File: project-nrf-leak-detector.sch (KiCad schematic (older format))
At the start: 16 parts, among them J1 Conn_02x05_Odd_Even, U1 MS88SF3_NRF52840

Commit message: Add a few more components to the schematic
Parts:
- added D?: D_Schottky, CUS10S30,H3F:DIO_CUS520,H3F, symbol Device:D_Schottky
- added L?: L, 22R686MC:INDP7870X750, symbol Device:L
- added Q?: Q_NMOS_GSD, Package_TO_SOT_SMD:SOT-323_SC-70, symbol Device:Q_NMOS_GSD
- added R?: 10k, Resistor_SMD:R_0603_1608Metric, symbol Device:R
- R1: value 5.1k -> 10k
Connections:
- net labels added: BUZZER, VBATT_PROBE, WATER_PROBE, ~RESET
- net labels removed: AIN0, AIN1, AIN2, AIN3, AIN5, NFC1, NFC2, P0.13, RESET
- wire segments 100 -> 98
- no-connect marks 28 -> 26
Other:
- note added: "Battery Voltage Reading"
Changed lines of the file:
@@
 $EndComp
 Text Label 1350 6600 0    50   ~ 0
-RESET
+~RESET
 $Comp
 L Device:R R1
@@
 P 1850 6350
 F 0 "R1" H 1920 6396 50  0000 L CNN
-F 1 "5.1k" H 1920 6305 50  0000 L CNN
+F 1 "10k" H 1920 6305 50  0000 L CNN
 F 2 "Resistor_SMD:R_0603_1608Metric" V 1780 6350 50  0001 C CNN
 F 3 "~" H 1850 6350 50  0001 C CNN
@@
 	3250 6600 3250 7100
 Text Label 6450 4550 2    50   ~ 0
-RESET
+~RESET
 Wire Wire Line
 	6450 4550 6100 4550
@@
 Wire Wire Line
 	3950 4400 3600 4400
-Text Label 850  2500 0    50   ~ 0
-AIN0
-Wire Wire Line
-	850  2500 1200 2500
-Text Label 3950 2700 2    50   ~ 0
-AIN5
-Wire Wire Line
-	3950 2700 3600 2700
-Text Label 850  2800 0    50   ~ 0
-AIN3
-Wire Wire Line
-	850  2800 1200 2800
-Text Label 850  2700 0    50   ~ 0
-AIN2
-Wire Wire Line
-	850  2700 1200 2700
-Text Label 850  3300 0    50   ~ 0
-NFC2
-Wire Wire Line
-	850  3300 1200 3300
-Text Label 850  3200 0    50   ~ 0
-NFC1
-Wire Wire Line
-	850  3200 1200 3200
+Text Label 650  2500 0    50   ~ 0
+WATER_PROBE
+Wire Wire Line
+	650  2500 1200 2500
+Text Label 650  2700 0    50   ~ 0
+VBATT_PROBE
+Wire Wire Line
+	650  2700 1200 2700
 Text Label 3950 2300 2    50   ~ 0
 P0.25
@@
 D_P
 Text Label 850  4100 0    50   ~ 0
-RESET
+~RESET
 Wire Wire Line
 	850  4100 1200 4100
@@
 Wire Wire Line
 	850  3800 1200 3800
-Text Label 850  3600 0    50   ~ 0
-P0.13
-Wire Wire Line
-	850  3600 1200 3600
+Text Label 850  2900 0    50   ~ 0
+BUZZER
+Wire Wire Line
+	850  2900 1200 2900
 Text Label 850  4200 0    50   ~ 0
 P0.19
@@
 	1    0    0    -1
 $EndComp
-Text Label 850  2600 0    50   ~ 0
-AIN1
-Wire Wire Line
-	850  2600 1200 2600
 NoConn ~ 1200 1800
 NoConn ~ 1200 2300
 NoConn ~ 1200 2400
-NoConn ~ 1200 2900
 NoConn ~ 1200 3000
 NoConn ~ 1200 3100
@@
 NoConn ~ 3600 2400
 NoConn ~ 3600 2500
-NoConn ~ 3600 2600
 NoConn ~ 3600 2800
 NoConn ~ 3600 2900
@@
 	1    0    0    -1
 $EndComp
+Text Notes 7050 3750 0    50   ~ 0
+Battery Voltage Reading
+Text Label 7200 4100 0    50   ~ 0
+VBATT_PROBE
+Wire Wire Line
+	7750 4100 7200 4100
+Text Label 9600 2700 0    50   ~ 0
+WATER_PROBE
+Wire Wire Line
+	9600 2700 10150 2700
+$Comp
+L Device:Q_NMOS_GSD Q?
+U 1 1 6387FC80
+P 5450 1900
+F 0 "Q?" H 5655 1900 50  0000 L CNN
+F 1 "Q_NMOS_GSD" H 5654 1855 50  0001 L CNN
+F 2 "Package_TO_SOT_SMD:SOT-323_SC-70" H 5650 2000 50  0001 C CNN
+F 3 "~" H 5450 1900 50  0001 C CNN
+	1    5450 1900
+	1    0    0    -1
+$EndComp
+$Comp
+L Device:D_Schottky D?
+U 1 1 6388212A
+P 5450 2550
+F 0 "D?" H 5450 2675 50  0000 C CNN
+F 1 "D_Schottky" H 5450 2676 50  0001 C CNN
+F 2 "CUS10S30,H3F:DIO_CUS520,H3F" H 5450 2550 50  0001 C CNN
+F 3 "~" H 5450 2550 50  0001 C CNN
+	1    5450 2550
+	1    0    0    -1
+$EndComp
+$Comp
+L Device:L L?
+U 1 1 638880E9
+P 6000 2400
+F 0 "L?" H 6053 2446 50  0000 L CNN
+F 1 "L" H 6053 2355 50  0000 L CNN
+F 2 "22R686MC:INDP7870X750" H 6000 2400 50  0001 C CNN
+F 3 "~" H 6000 2400 50  0001 C CNN
+	1    6000 2400
+	1    0    0    -1
+$EndComp
+$Comp
+L Device:R R?
+U 1 1 6388DC50
+P 4950 2150
+F 0 "R?" H 5020 2196 50  0000 L CNN
+F 1 "10k" H 5020 2105 50  0000 L CNN
+F 2 "Resistor_SMD:R_0603_1608Metric" V 4880 2150 50  0001 C CNN
+F 3 "~" H 4950 2150 50  0001 C CNN
+	1    4950 2150
+	1    0    0    -1
+$EndComp
+$Comp
+L power:GND #PWR?
+U 1 1 63892E4C
+P 4950 2450
+F 0 "#PWR?" H 4950 2200 50  0001 C CNN
+F 1 "GND" H 4955 2277 50  0000 C CNN
+F 2 "" H 4950 2450 50  0001 C CNN
+F 3 "" H 4950 2450 50  0001 C CNN
+	1    4950 2450
+	1    0    0    -1
+$EndComp
+Text Label 4800 1650 0    50   ~ 0
+BUZZER
+Wire Wire Line
+	4800 1650 5150 1650
 $EndSCHEMATC

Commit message: First schematic version
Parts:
- removed C6: 4.7uF, Capacitor_SMD:C_0805_2012Metric, symbol Device:C
- removed JP1: SolderJumper_2_Bridged, Jumper:SolderJumper-2_P1.3mm_Bridged_RoundedPad1.0x1.5mm, symbol Jumper:SolderJumper_2_Bridged
- removed JP2: SolderJumper_2_Open, Jumper:SolderJumper-2_P1.3mm_Open_RoundedPad1.0x1.5mm, symbol Jumper:SolderJumper_2_Open
- removed L1: 10uH, Inductor_SMD:L_0603_1608Metric, symbol Device:L
- removed R3: 4.7, Resistor_SMD:R_0603_1608Metric, symbol Device:R
- added R?: 10k, Resistor_SMD:R_0603_1608Metric, symbol Device:R
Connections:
- net labels added: VDD
- net labels removed: DCCH, D_N, D_P, P0.15, P0.17, P0.19, P0.21, P0.22, P0.23, P0.25, P1.10, P1.13, P1.14, P1.15, VBATT_PROBE, VBUS, VBUS_nRF, VDDH
- wire segments 98 -> 71
- no-connect marks 26 -> 47
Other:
- note added: "Normal Voltage Mode\nLDO only"
- note removed: "(VDD OUT)"
- note removed: "Battery Voltage Reading"
- note removed: "PCA10059\nRevision: 2.0.0\n17.09.2020"
- note removed: "Power Input Choice"
- moved on the sheet: BT?, C2, D?, J?, L?, LS?, Q?, R?

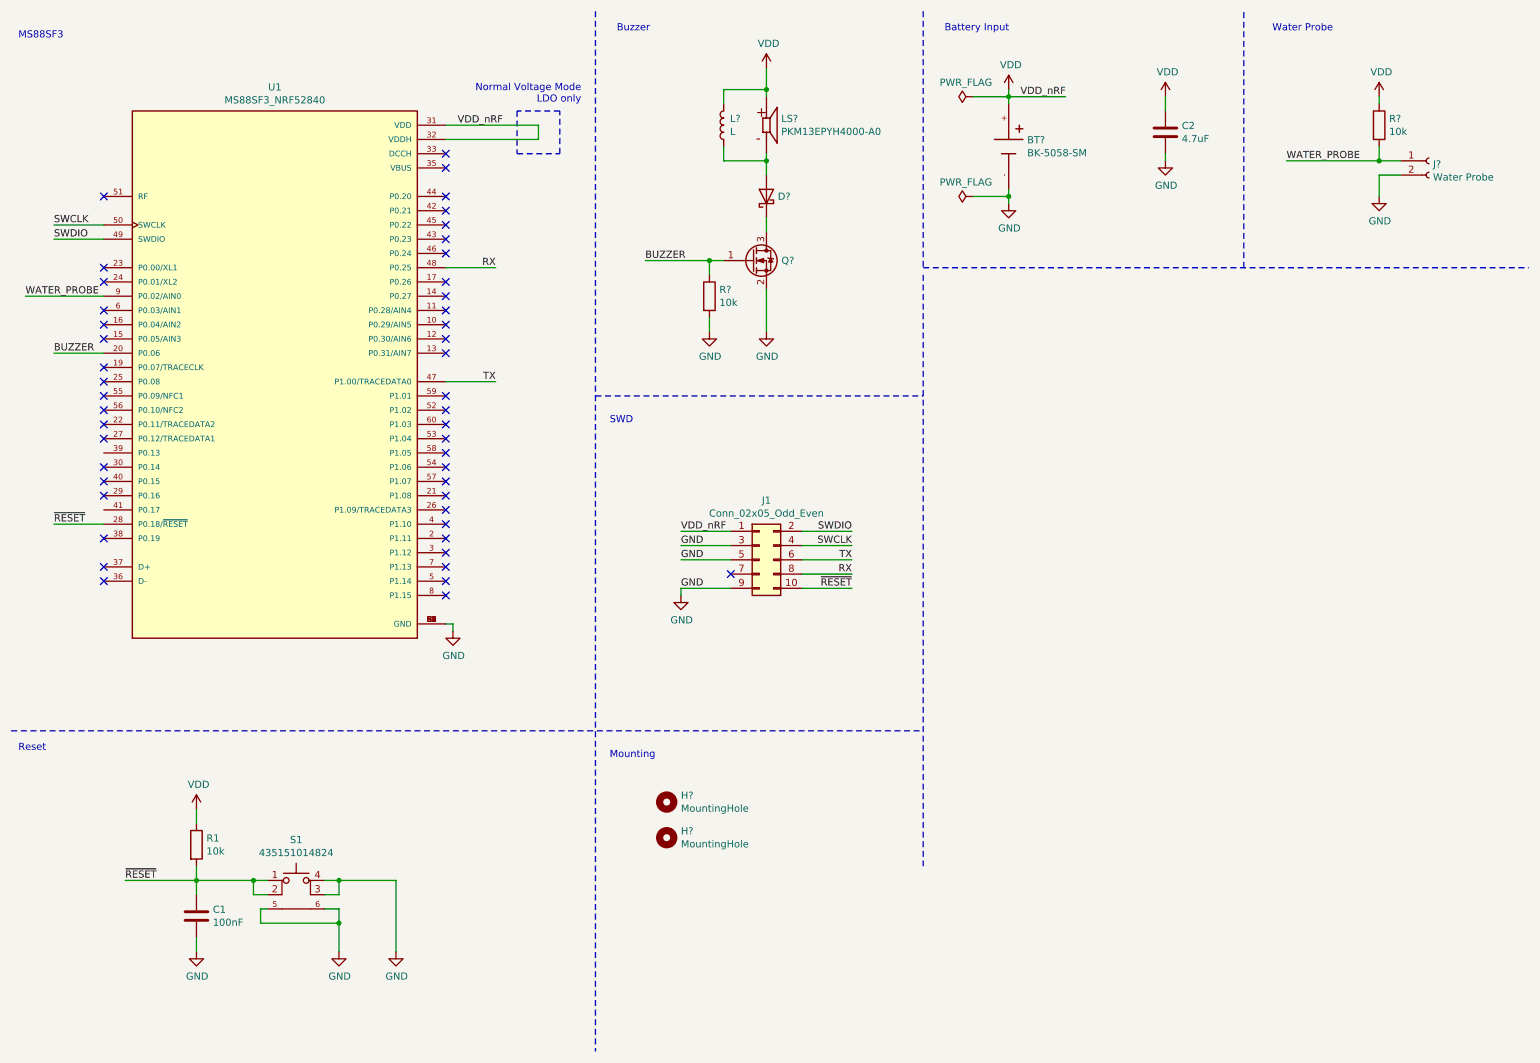
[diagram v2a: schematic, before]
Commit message: Import parts to board
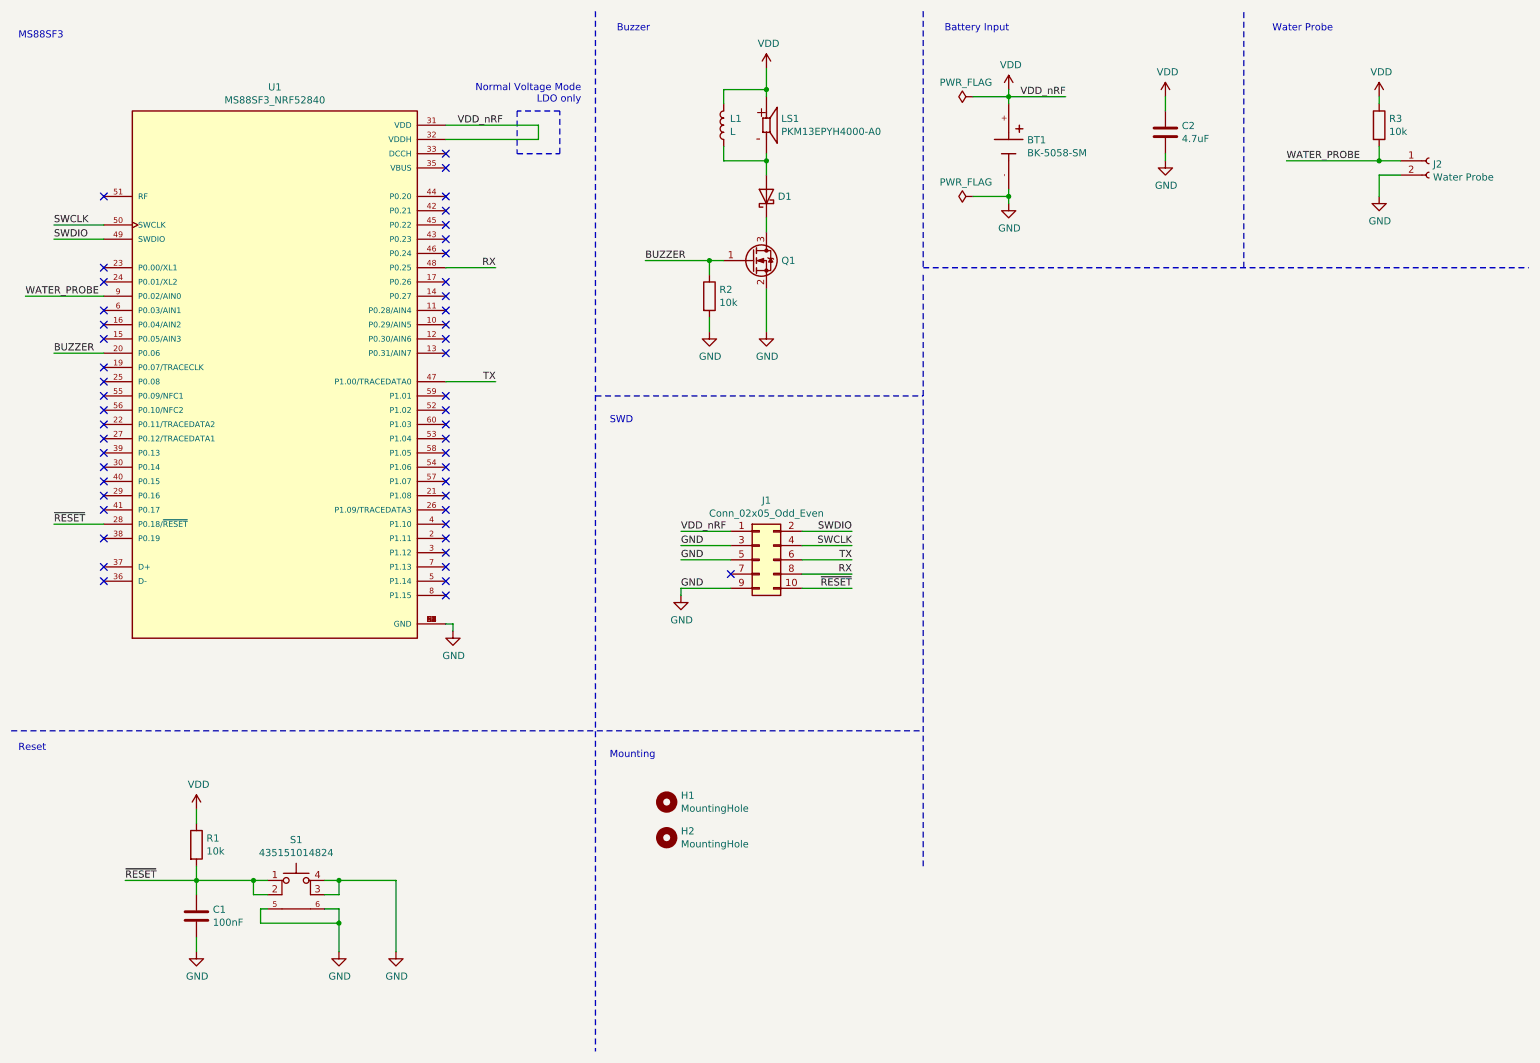
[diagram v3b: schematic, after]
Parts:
- LS1: renamed from LS?; footprint PKM13EPYH4000-A0:SPKR_PKM13EPYH4000-A0 -> PKM13EPYH4000-A0:SPKR_PKM13EPYH4000-A0_SMD
- gave numbers to parts that had none: 9
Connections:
- no-connect marks 47 -> 49
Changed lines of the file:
@@
 $EndDescr
 $Comp
-L Mechanical:MountingHole H?
+L Mechanical:MountingHole H1
 U 1 1 6372E32E
 P 5150 6050
-F 0 "H?" H 5250 6096 50  0000 L CNN
+F 0 "H1" H 5250 6096 50  0000 L CNN
 F 1 "MountingHole" H 5250 6005 50  0000 L CNN
 F 2 "MountingHole:MountingHole_5mm" H 5150 6050 50  0001 C CNN
@@
 $EndComp
 $Comp
-L Mechanical:MountingHole H?
+L Mechanical:MountingHole H2
 U 1 1 6372E6D4
 P 5150 6300
-F 0 "H?" H 5250 6346 50  0000 L CNN
+F 0 "H2" H 5250 6346 50  0000 L CNN
 F 1 "MountingHole" H 5250 6255 50  0000 L CNN
 F 2 "MountingHole:MountingHole_5mm" H 5150 6300 50  0001 C CNN
@@
 $EndComp
 $Comp
-L PKM13EPYH4000-A0:PKM13EPYH4000-A0 LS?
+L PKM13EPYH4000-A0:PKM13EPYH4000-A0 LS1
 U 1 1 6372EE2A
 P 5850 1300
-F 0 "LS?" H 5954 1346 50  0000 L CNN
+F 0 "LS1" H 5954 1346 50  0000 L CNN
 F 1 "PKM13EPYH4000-A0" H 5954 1255 50  0000 L CNN
-F 2 "PKM13EPYH4000-A0:SPKR_PKM13EPYH4000-A0" H 5850 1300 50  0001 L BNN
+F 2 "PKM13EPYH4000-A0:SPKR_PKM13EPYH4000-A0_SMD" H 5850 1300 50  0001 L BNN
 F 3 "" H 5850 1300 50  0001 L BNN
 F 4 "December 26, 2017" H 5850 1300 50  0001 L BNN "PARTREV"
@@
 $EndComp
 $Comp
-L BK-5058-SM:BK-5058-SM BT?
+L BK-5058-SM:BK-5058-SM BT1
 U 1 1 637D595F
 P 7550 1450
-F 0 "BT?" V 7504 1580 50  0000 L CNN
+F 0 "BT1" V 7504 1580 50  0000 L CNN
 F 1 "BK-5058-SM" V 7595 1580 50  0000 L CNN
 F 2 "BK-5058-SM:BAT_BK-5058-SM" H 7650 2050 50  0001 L BNN
@@
 $EndComp
 $Comp
-L Device:Q_NMOS_GSD Q?
+L Device:Q_NMOS_GSD Q1
 U 1 1 6387FC80
 P 5750 2250
-F 0 "Q?" H 5955 2250 50  0000 L CNN
+F 0 "Q1" H 5955 2250 50  0000 L CNN
 F 1 "Q_NMOS_GSD" H 5954 2205 50  0001 L CNN
 F 2 "Package_TO_SOT_SMD:SOT-323_SC-70" H 5950 2350 50  0001 C CNN
@@
 $EndComp
 $Comp
-L Device:L L?
+L Device:L L1
 U 1 1 638880E9
 P 5550 1300
-F 0 "L?" H 5506 1254 50  0000 R CNN
+F 0 "L1" H 5506 1254 50  0000 R CNN
 F 1 "L" H 5506 1345 50  0000 R CNN
 F 2 "22R686MC:INDP7870X750" H 5550 1300 50  0001 C CNN
@@
 $EndComp
 $Comp
-L Device:R R?
+L Device:R R2
 U 1 1 6388DC50
 P 5450 2500
-F 0 "R?" H 5520 2546 50  0000 L CNN
+F 0 "R2" H 5520 2546 50  0000 L CNN
 F 1 "10k" H 5520 2455 50  0000 L CNN
 F 2 "Resistor_SMD:R_0603_1608Metric" V 5380 2500 50  0001 C CNN
@@
 Normal Voltage Mode\nLDO only
 $Comp
-L Device:R R?
+L Device:R R3
 U 1 1 63F7A9F2
 P 10150 1300
-F 0 "R?" H 10220 1346 50  0000 L CNN
+F 0 "R3" H 10220 1346 50  0000 L CNN
 F 1 "10k" H 10220 1255 50  0000 L CNN
 F 2 "Resistor_SMD:R_0603_1608Metric" V 10080 1300 50  0001 C CNN
@@
 	10150 1650 10300 1650
 $Comp
-L Connector:Conn_01x02_Female J?
+L Connector:Conn_01x02_Female J2
 U 1 1 637340AC
 P 10500 1550
-F 0 "J?" H 10528 1526 50  0000 L CNN
+F 0 "J2" H 10528 1526 50  0000 L CNN
 F 1 "Water Probe" H 10528 1435 50  0000 L CNN
 F 2 "TZ022101B000G:TZ022101B000G" H 10500 1550 50  0001 C CNN
@@
 $EndComp
 $Comp
-L Device:D_Schottky D?
+L Device:D_Schottky D1
 U 1 1 6388212A
 P 5850 1800
-F 0 "D?" V 5850 1720 50  0000 R CNN
+F 0 "D1" V 5850 1720 50  0000 R CNN
 F 1 "D_Schottky" H 5850 1926 50  0001 C CNN
 F 2 "CUS10S30,H3F:DIO_CUS520,H3F" H 5850 1800 50  0001 C CNN
@@
 Wire Notes Line
 	9200 2300 9200 500
+NoConn ~ 1200 3600
+NoConn ~ 1200 4000
 $EndSCHEMATC

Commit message: First placement
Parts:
- removed BT1: BK-5058-SM, BK-5058-SM:BAT_BK-5058-SM, symbol BK-5058-SM:BK-5058-SM
- added BT1: BK-912-TR, BK-912:MPD_BK-912-TR, symbol BK-912-TR:BK-912-TR
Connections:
- net GND: now also BT1.2 (-)
- net VDD: now also BT1.1 (+)
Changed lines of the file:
@@
-$EndComp
-$Comp
-L BK-5058-SM:BK-5058-SM BT1
-U 1 1 637D595F
-P 7550 1450
-F 0 "BT1" V 7504 1580 50  0000 L CNN
-F 1 "BK-5058-SM" V 7595 1580 50  0000 L CNN
-F 2 "BK-5058-SM:BAT_BK-5058-SM" H 7650 2050 50  0001 L BNN
-F 3 "" H 7550 1450 50  0001 L BNN
-F 4 "20.83mm" H 7650 1850 50  0001 L BNN "MAXIMUM_PACKAGE_HEIGHT"
-F 5 "MPD" H 7650 2150 50  0001 L BNN "MANUFACTURER"
-F 6 "C" H 7650 1750 50  0001 L BNN "PARTREV"
-F 7 "Manufacturer Recommendations" H 7650 1950 50  0001 L BNN "STANDARD"
-	1    7550 1450
-	0    1    1    0
 $EndComp
 $Comp
@@
 	7550 1050 7550 1100
 Wire Wire Line
-	7550 1750 7550 1800
-Wire Wire Line
 	7300 1100 7550 1100
 Connection ~ 7550 1100
-Wire Wire Line
-	7550 1100 7550 1150
 Wire Wire Line
 	7300 1800 7550 1800
@@
 NoConn ~ 1200 3600
 NoConn ~ 1200 4000
+$Comp
+L BK-912-TR:BK-912-TR BT1
+U 1 1 6407499C
+P 7550 1450
+F 0 "BT1" V 7596 1317 50  0000 R CNN
+F 1 "BK-912-TR" V 7505 1317 50  0000 R CNN
+F 2 "BK-912:MPD_BK-912-TR" H 7650 1950 50  0001 L BNN
+F 3 "" H 7550 1450 50  0001 L BNN
+F 4 "Manufacturer Recommendations" H 7650 1850 50  0001 L BNN "STANDARD"
+F 5 "H" H 7650 2050 50  0001 L BNN "PARTREV"
+F 6 "MPD" H 7650 1750 50  0001 L BNN "MANUFACTURER"
+	1    7550 1450
+	0    -1   -1   0
+$EndComp
+Wire Wire Line
+	7550 1100 7550 1250
+Wire Wire Line
+	7550 1650 7550 1800
 $EndSCHEMATC

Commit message: First routing
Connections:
- net WATER_PROBE: now also U1.16 (P0.04/AIN2); no longer U1.9 (P0.02/AIN0)
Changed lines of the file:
@@
 Wire Wire Line
 	6100 4450 6450 4450
-Text Label 650  2500 0    50   ~ 0
-WATER_PROBE
-Wire Wire Line
-	650  2500 1200 2500
 Text Label 850  4100 0    50   ~ 0
 ~RESET
@@
 Wire Wire Line
 	850  2100 1200 2100
-Text Label 850  2900 0    50   ~ 0
+Text Label 650  2900 0    50   ~ 0
 BUZZER
-Wire Wire Line
-	850  2900 1200 2900
 Wire Wire Line
 	8650 1500 8650 1550
@@
 	5850 1950 5850 2050
 NoConn ~ 1200 2600
-NoConn ~ 1200 2700
 NoConn ~ 1200 2800
 NoConn ~ 1200 3200
 NoConn ~ 1200 3300
 NoConn ~ 1200 3800
-NoConn ~ 1200 4200
 NoConn ~ 1200 4400
 NoConn ~ 1200 4500
@@
 Wire Wire Line
 	7550 1650 7550 1800
+NoConn ~ 1200 4200
+Wire Wire Line
+	650  2700 1200 2700
+Text Label 650  2700 0    50   ~ 0
+WATER_PROBE
+NoConn ~ 1200 2500
+Wire Wire Line
+	650  2900 1200 2900
 $EndSCHEMATC

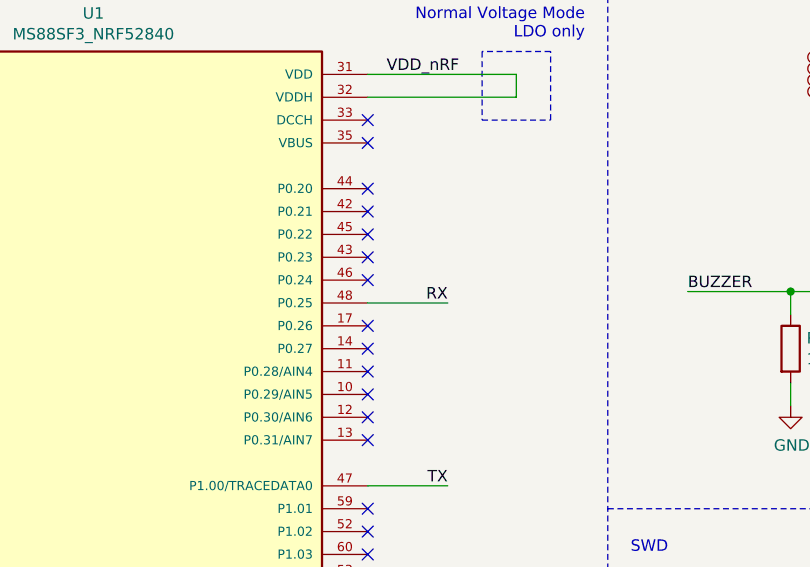
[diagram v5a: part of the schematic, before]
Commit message: Change RX pin to P0.24
To avoid crossing over TX.
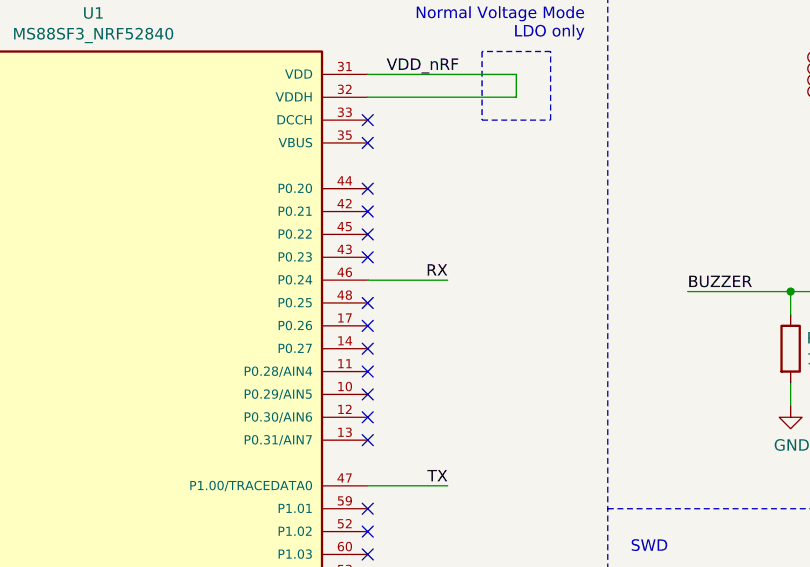
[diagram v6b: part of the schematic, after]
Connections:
- net RX: now also U1.46 (P0.24); no longer U1.48 (P0.25)
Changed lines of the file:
@@
 TX
 Wire Wire Line
-	3950 2300 3600 2300
-Text Label 3950 2300 2    50   ~ 0
+	3950 2200 3600 2200
+Text Label 3950 2200 2    50   ~ 0
 RX
 $Comp
@@
 NoConn ~ 3600 2000
 NoConn ~ 3600 2100
-NoConn ~ 3600 2200
+NoConn ~ 3600 2300
 NoConn ~ 3600 2600
 NoConn ~ 3600 2700
